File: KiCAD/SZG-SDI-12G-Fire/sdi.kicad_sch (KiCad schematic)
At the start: 49 parts, among them U2 GS12241-INE3, U3 GS12281-INTE3

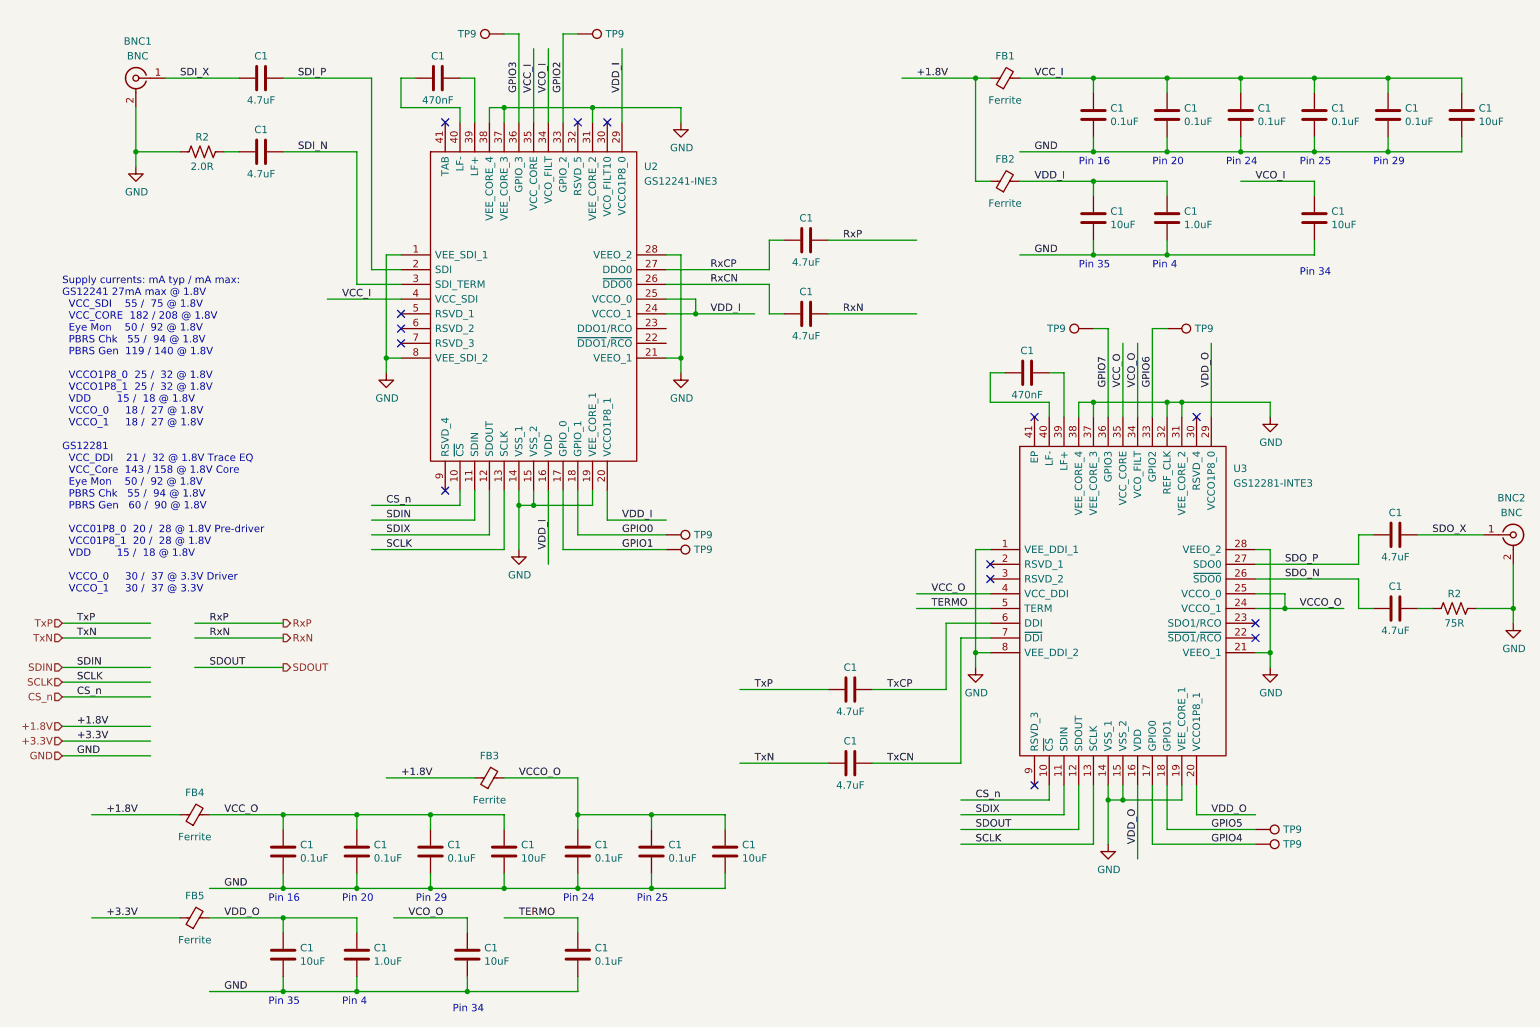
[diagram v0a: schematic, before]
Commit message: Initial version: Rev.A
Minor schematic tweaks for routing and to address SDI Rx/Tx power rails
PCB fully placed and routed
Added README/CHANGES files
Added CERN-OHL-P v2 license file

Signed-off-by: Charles Steinkuehler <charles@steinkuehler.net>
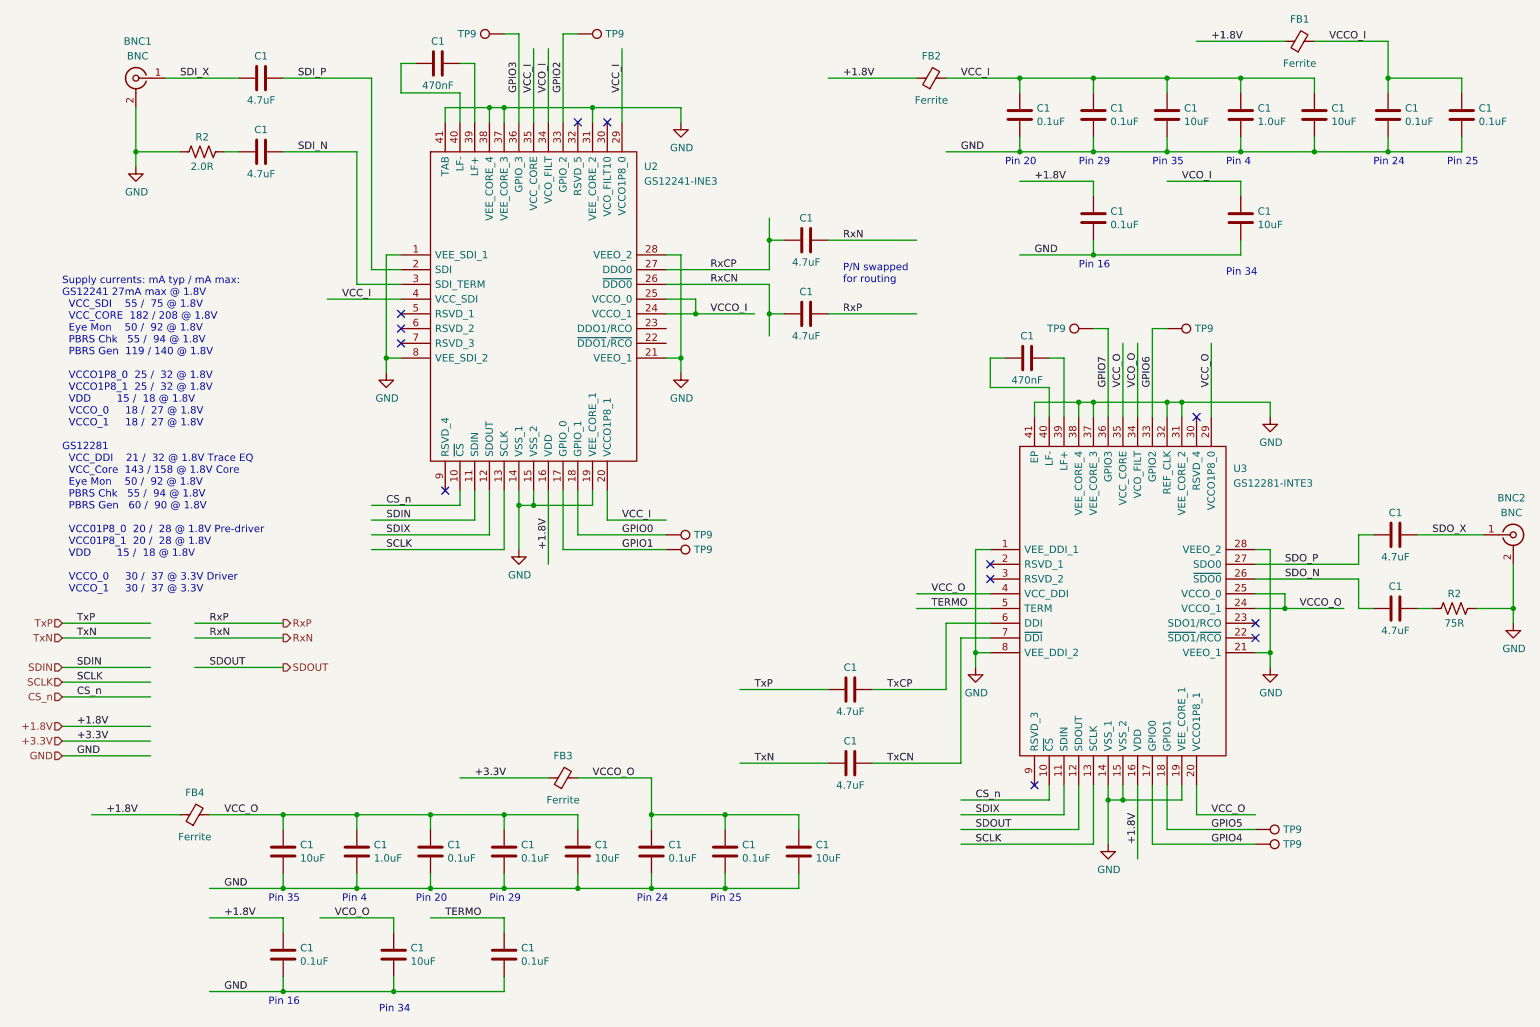
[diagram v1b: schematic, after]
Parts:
- removed FB5: Ferrite, SYZYGY:BEADC1005X55N, symbol Device:FerriteBead_Small
- TP9: footprint SYZYGY:TestPoint-20mil -> TestPoint:TestPoint_THTPad_D1.0mm_Drill0.5mm
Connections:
- net +1.8V: now also C1.1, C1.1, U2.16 (VDD), U3.16 (VDD); no longer FB3.1
- net +3.3V: now also FB3.1
- net GND: now also U2.41 (TAB), U3.41 (EP)
- net RxN: now also C1.2; no longer C1.2
- net RxP: now also C1.2; no longer C1.2
- net VCC_I: now also C1.1, C1.1, FB2.2, U2.20 (VCCO1P8_1), U2.29 (VCCO1P8_0); no longer C1.1, C1.1, C1.1, FB1.2
- net VCC_O: now also C1.1, C1.1, U3.20 (VCCO1P8_1), U3.29 (VCCO1P8_0); no longer C1.1
- removed net VDD_I: C1.1, C1.1, FB2.2, U2.16 (VDD), U2.20 (VCCO1P8_1), U2.24 (VCCO_1), U2.25 (VCCO_0), U2.29 (VCCO1P8_0)
- removed net VDD_O: C1.1, C1.1, U3.16 (VDD), U3.20 (VCCO1P8_1), U3.29 (VCCO1P8_0)
- new net VCCO_I: C1.1, C1.1, FB1.2, U2.24 (VCCO_1), U2.25 (VCCO_0)
- no-connect marks 14 -> 12
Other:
- note added: "P/N swapped for routing"
- moved on the sheet: C1, FB1, FB2, FB3

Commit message: Update with part numbers
Add manufacturer part numbers as ordered from DigiKey
Add stitching vias on PCB for SDI 75 ohm striplines

Signed-off-by: Charles Steinkuehler <charles@steinkuehler.net>
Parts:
- C1: Manufacturer (none) -> Murata; Manufacturer_PN (none) -> GRM155R71E104KE14J
- C1: Manufacturer (none) -> Murata; Manufacturer_PN (none) -> GRM155R60J475ME47D
- C1: Manufacturer (none) -> Murata; Manufacturer_PN (none) -> GRM155R71A474ME01D
- C1: Manufacturer (none) -> Murata; Manufacturer_PN (none) -> GRM155R60J106ME05D
- C1: Manufacturer (none) -> Murata; Manufacturer_PN (none) -> GRM155R70J105KA12J
- R2: Manufacturer (none) -> Yageo; Manufacturer_PN (none) -> RC0402FR-072RL
- R2: Manufacturer (none) -> Yageo; Manufacturer_PN (none) -> RC0402FR-0775RL
